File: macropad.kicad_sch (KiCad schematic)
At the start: 1 part, among them U1 MOUDLE-SEEEDUINO-XIAO

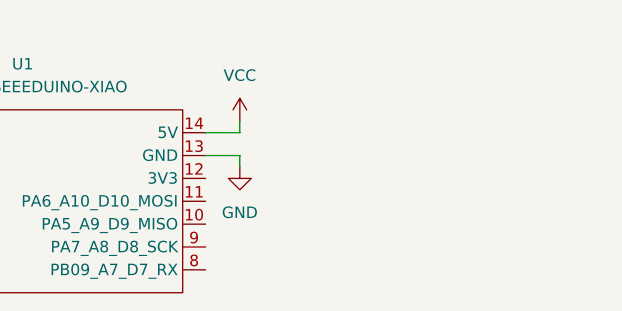
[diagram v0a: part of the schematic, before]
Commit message: sch done + pcb planning
fixed all footprints. might delete vcc at top later
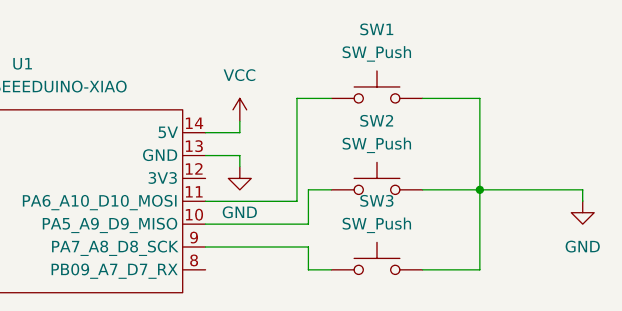
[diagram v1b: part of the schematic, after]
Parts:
- added SW1, SW2, SW3: SW_Push, Button_Switch_Keyboard:SW_Cherry_MX_1.00u_PCB, symbol Switch:SW_Push
- U1: footprint (none) -> XIAO_PCB:XIAO-Generic-Hybrid-14P-2.54-21X17.8MM
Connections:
- net GND: now also SW1.2, SW2.2, SW3.2
- net at U1.10 (PA5_A9_D9_MISO): now also SW2.1
- net at U1.11 (PA6_A10_D10_MOSI): now also SW1.1
- net at U1.9 (PA7_A8_D8_SCK): now also SW3.1

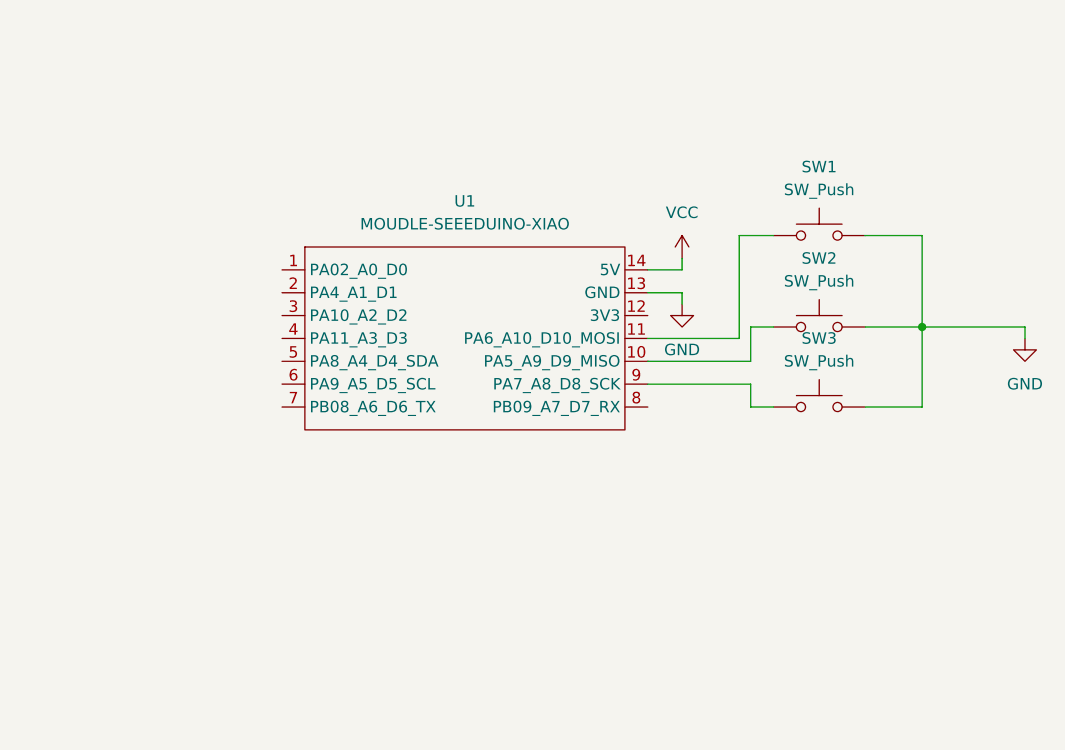
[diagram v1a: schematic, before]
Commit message: need to fix errors
so far i have 3 keys, one rotary encoder, and an oled screen
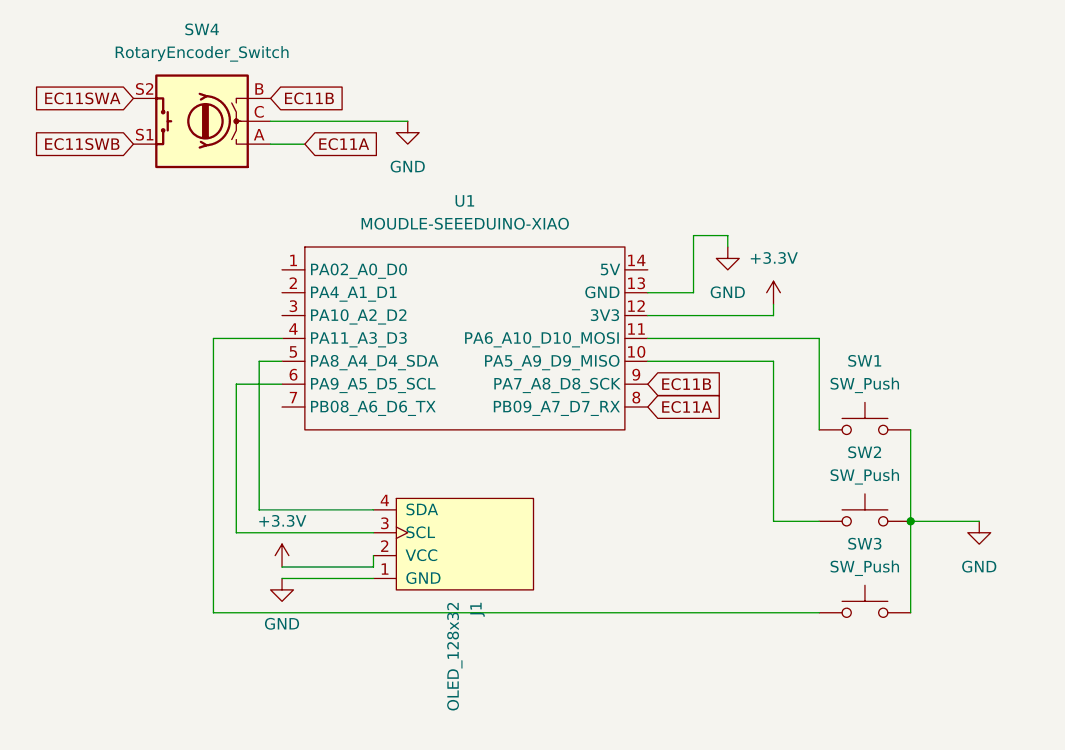
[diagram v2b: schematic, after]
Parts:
- added J1: OLED_128x32, XIAO_PCB:OLED_128x32, symbol ScottoKeebs:OLED_128x32
- added SW4: RotaryEncoder_Switch, Rotary_Encoder:RotaryEncoder_Alps_EC11E-Switch_Vertical_H20mm, symbol Device:RotaryEncoder_Switch
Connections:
- net GND: now also J1.1 (GND), SW4.C
- net at SW3.1: now also U1.4 (PA11_A3_D3); no longer U1.9 (PA7_A8_D8_SCK)
- net +3.3V: now reaches U1.12 (3V3)
- net +3.3V: now also J1.2 (VCC)
- net at U1.5 (PA8_A4_D4_SDA): now also J1.4 (SDA)
- net at U1.6 (PA9_A5_D5_SCL): now also J1.3 (SCL)
- net EC11A: now reaches U1.8 (PB09_A7_D7_RX)
- net EC11A: now also SW4.A
- net VCC: no longer names the net of U1.14 (5V)
- new net EC11B: SW4.B, U1.9 (PA7_A8_D8_SCK)
- new net EC11SWA: SW4.S2
- new net EC11SWB: SW4.S1

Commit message: final fixes on pcb + sch files
can't wait to start the model!
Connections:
- net EC11SWA is gone; now on an unnamed net: SW4.S2
- net EC11SWB is gone; now on net GND: SW4.S1
- no-connect marks 0 -> 4
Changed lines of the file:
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@@
 		(color 0 0 0 0)
 	)
+	(no_connect
+		(at 106.68 72.39)
+	)
+	(no_connect
+		(at 66.04 74.93)
+	)
+	(no_connect
+		(at 66.04 77.47)
+	)
+	(no_connect
+		(at 66.04 87.63)
+	)
+	(wire
+		(pts
+			(xy 49.53 53.34) (xy 38.1 53.34)
+		)
+		(stroke
+			(width 0)
+			(type default)
+		)
+	)
 	(wire
 		(pts
@@
 	(wire
 		(pts
+			(xy 38.1 53.34) (xy 38.1 72.39)
+		)
+		(stroke
+			(width 0)
+			(type default)
+		)
+	)
+	(wire
+		(pts
 			(xy 76.2 101.6) (xy 60.96 101.6)
 		)
@@
 		(pts
 			(xy 111.76 68.58) (xy 115.57 68.58)
+		)
+		(stroke
+			(width 0)
+			(type default)
+		)
+	)
+	(wire
+		(pts
+			(xy 45.72 58.42) (xy 49.53 58.42)
+		)
+		(stroke
+			(width 0)
+			(type default)
+		)
+	)
+	(wire
+		(pts
+			(xy 38.1 72.39) (xy 66.04 72.39)
 		)
 		(stroke
@@
 				)
 				(justify left)
-				(hide yes)
-			)
-		)
-	)
-	(global_label "EC11SWB"
-		(shape input)
-		(at 49.53 58.42 180)
-		(fields_autoplaced yes)
-		(effects
-			(font
-				(size 1.27 1.27)
-			)
-			(justify right)
-		)
-		(property "Intersheetrefs" "${INTERSHEET_REFS}"
-			(at 37.7759 58.42 0)
-			(effects
-				(font
-					(size 1.27 1.27)
-				)
-				(justify right)
-				(hide yes)
-			)
-		)
-	)
-	(global_label "EC11SWA"
-		(shape input)
-		(at 49.53 53.34 180)
-		(fields_autoplaced yes)
-		(effects
-			(font
-				(size 1.27 1.27)
-			)
-			(justify right)
-		)
-		(property "Intersheetrefs" "${INTERSHEET_REFS}"
-			(at 37.9573 53.34 0)
-			(effects
-				(font
-					(size 1.27 1.27)
-				)
-				(justify right)
 				(hide yes)
 			)
@@
 					(unit 1)
 				)
+			)
+		)
+	)
+	(symbol
+		(lib_id "power:GND")
+		(at 45.72 58.42 0)
+		(unit 1)
+		(exclude_from_sim no)
+		(in_bom yes)
+		(on_board yes)
+		(dnp no)
+		(fields_autoplaced yes)
+		(property "Reference" "#PWR07"
+			(at 45.72 64.77 0)
+			(effects
+				(font
+					(size 1.27 1.27)
+				)
+				(hide yes)
+			)
+		)
+		(property "Value" "GND"
+			(at 45.72 63.5 0)
+			(effects
+				(font
+					(size 1.27 1.27)
+				)
+			)
+		)
+		(property "Footprint" ""
+			(at 45.72 58.42 0)
+			(effects
+				(font
+					(size 1.27 1.27)
+				)
+				(hide yes)
+			)
+		)
+		(property "Datasheet" ""
+			(at 45.72 58.42 0)
+			(effects
+				(font
+					(size 1.27 1.27)
+				)
+				(hide yes)
+			)
+		)
+		(property "Description" "Power symbol creates a global label with name \"GND\" , ground"
+			(at 45.72 58.42 0)
+			(effects
+				(font
+					(size 1.27 1.27)
+				)
+				(hide yes)
+			)
+		)
+		(pin "1"
+		)
+		(instances
+			(project ""
+				(path "/158bd223-f537-495a-a791-c7f77550fea3"
+					(reference "#PWR07")
+					(unit 1)
+				)

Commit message: changing to simple 3 keys wip
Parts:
- removed J1: OLED_128x32, XIAO_PCB:OLED_128x32, symbol ScottoKeebs:OLED_128x32
- removed SW4: RotaryEncoder_Switch, Rotary_Encoder:RotaryEncoder_Alps_EC11E-Switch_Vertical_H20mm, symbol Device:RotaryEncoder_Switch
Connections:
- net at U1.4 (PA11_A3_D3): no longer SW3.1
- net EC11A: no longer names the net of U1.8 (PB09_A7_D7_RX)
- net EC11B: no longer names the net of U1.9 (PA7_A8_D8_SCK)
- net EC11B: now also SW3.1
- no-connect marks 4 -> 10
